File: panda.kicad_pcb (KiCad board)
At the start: 2 copper layers, 144.8 x 38.1 mm, 30 parts, among them J1 USB, J2 ICSP, U1 ATMEGA328-P, U2 MAX7219, Y1 12MHz

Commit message: Cleanup and wording.
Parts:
- added REF**: Symbol_CreativeCommons_CopperTop_Type2_Small, Symbols:Symbol_CreativeCommons_CopperTop_Type2_Small, B.Cu at (195.6, 99.1)
- added REF**: Symbol_CreativeCommons_CopperTop_Type2_Small, Symbols:Symbol_CreativeCommons_CopperTop_Type2_Small, F.Cu at (59.7, 100.3)
- LED1, LED2, LED3, LED4: footprint LEDs:LED-5MM -> MyLEDs:LED-5MM
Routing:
- net ROW6: track 136.7 -> 130.7 mm
- net ROW5: track 89.5 -> 92.1 mm
- net ROW4: track 73.5 -> 74.3 mm
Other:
- board text added: "Original design by Spare Time Gizmos 2004. USB redesign by David Griffith 2015"
- board text added: "Panda Display Panel USB Edition"

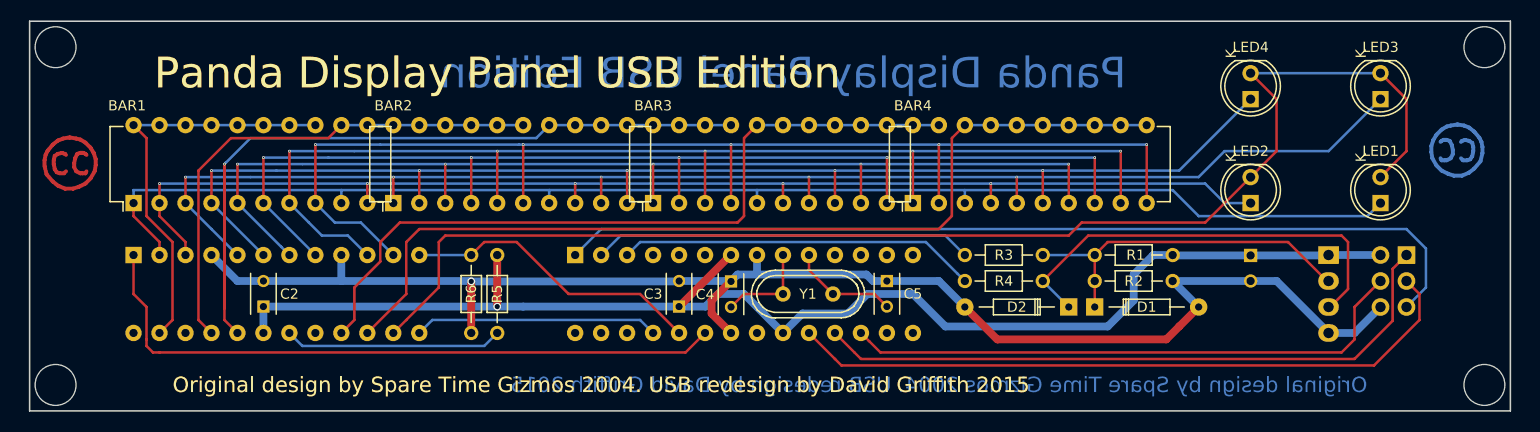
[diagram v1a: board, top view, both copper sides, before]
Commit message: Enlarge vias and added blurbs.
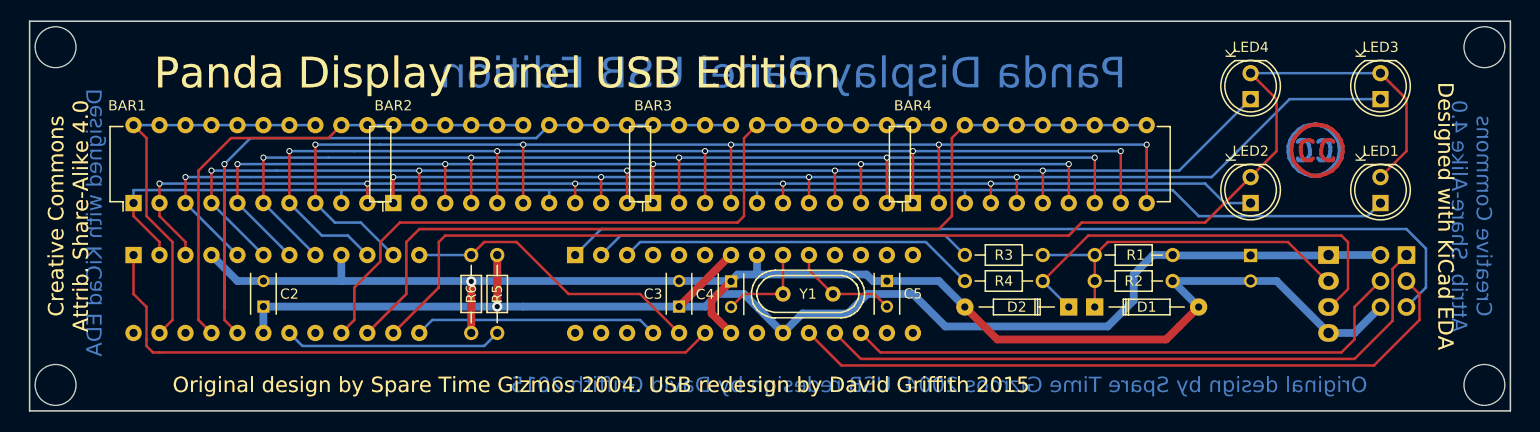
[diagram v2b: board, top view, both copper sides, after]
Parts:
- moved REF** 121.9 mm to (181.6, 99.1)
- moved REF** 14.0 mm to (181.6, 99.1)
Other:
- board text added: "Creative Commons Attrib. Share-Alike 4.0"
- board text added: "Designed with KiCad EDA"

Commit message: Minor aesthetic tweak.
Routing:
- net COL1: track 136.0 -> 135.2 mm
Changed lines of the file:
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@@
     (thickness 1.6)
     (drawings 18)
-    (tracks 371)
+    (tracks 370)
     (zones 0)
     (modules 32)
@@
   )
   (layers
-    (0 F.Cu signal)
-    (31 B.Cu signal hide)
+    (0 F.Cu signal hide)
+    (31 B.Cu signal)
     (32 B.Adhes user)
     (33 F.Adhes user)
@@
   )
   (gr_line (start 55.88 124.46) (end 55.88 86.36) (layer Edge.Cuts) (width 0.15))
+  (segment (start 66.04 104.14) (end 67.31 102.87) (width 0.25) (layer B.Cu) (net 1))
+  (segment (start 67.31 102.87) (end 86.36 102.87) (width 0.25) (layer B.Cu) (net 1))
   (segment (start 147.32 102.87) (end 167.64 102.87) (width 0.25) (layer B.Cu) (net 1))
   (segment (start 167.64 102.87) (end 170.185001 105.415001) (width 0.25) (layer B.Cu) (net 1))
@@
   (segment (start 66.04 105.41) (end 66.04 104.14) (width 0.25) (layer F.Cu) (net 1))
   (segment (start 68.58 109.22) (end 68.58 107.95) (width 0.25) (layer F.Cu) (net 1))
-  (segment (start 67.31 102.87) (end 86.36 102.87) (width 0.25) (layer B.Cu) (net 1))
-  (segment (start 66.04 102.87) (end 67.31 102.87) (width 0.25) (layer B.Cu) (net 1))
   (segment (start 147.32 102.87) (end 147.32 104.14) (width 0.25) (layer B.Cu) (net 1))
   (segment (start 127 102.87) (end 147.32 102.87) (width 0.25) (layer B.Cu) (net 1))
@@
   (segment (start 86.36 102.87) (end 106.68 102.87) (width 0.25) (layer B.Cu) (net 1))
   (segment (start 86.36 102.87) (end 86.36 104.14) (width 0.25) (layer B.Cu) (net 1))
-  (segment (start 66.04 104.14) (end 66.04 102.87) (width 0.25) (layer B.Cu) (net 1))
   (via (at 149.86 102.235) (size 0.6) (drill 0.4) (layers F.Cu B.Cu) (net 2))
   (via (at 129.54 102.235) (size 0.6) (drill 0.4) (layers F.Cu B.Cu) (net 2))

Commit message: Even more tweaks.
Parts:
- removed the REF** at (181.6, 99.1) (x2)
- added REF**: Symbol_OSHW-Logo_CopperTop, Symbols:Symbol_OSHW-Logo_CopperTop, B.Cu at (181.6, 96.5)
- added REF**: Symbol_OSHW-Logo_CopperTop, Symbols:Symbol_OSHW-Logo_CopperTop, F.Cu at (181.6, 96.5)
- added REF**: Symbol_OSHW-Logo_SilkScreen, Symbols:Symbol_OSHW-Logo_SilkScreen, F.Cu at (181.6, 96.5)
- added REF**: Symbol_OSHW-Logo_SilkScreen, Symbols:Symbol_OSHW-Logo_SilkScreen, B.Cu at (181.6, 96.5)
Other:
- board text added: "Blinkenlights panel for PDP-10 emulators"
